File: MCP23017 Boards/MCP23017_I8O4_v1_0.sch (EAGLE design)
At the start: 71 parts, among them IC3 74HC540N, IC4 74HC540N, IC5 MCP23017SP, X4 057-016-0

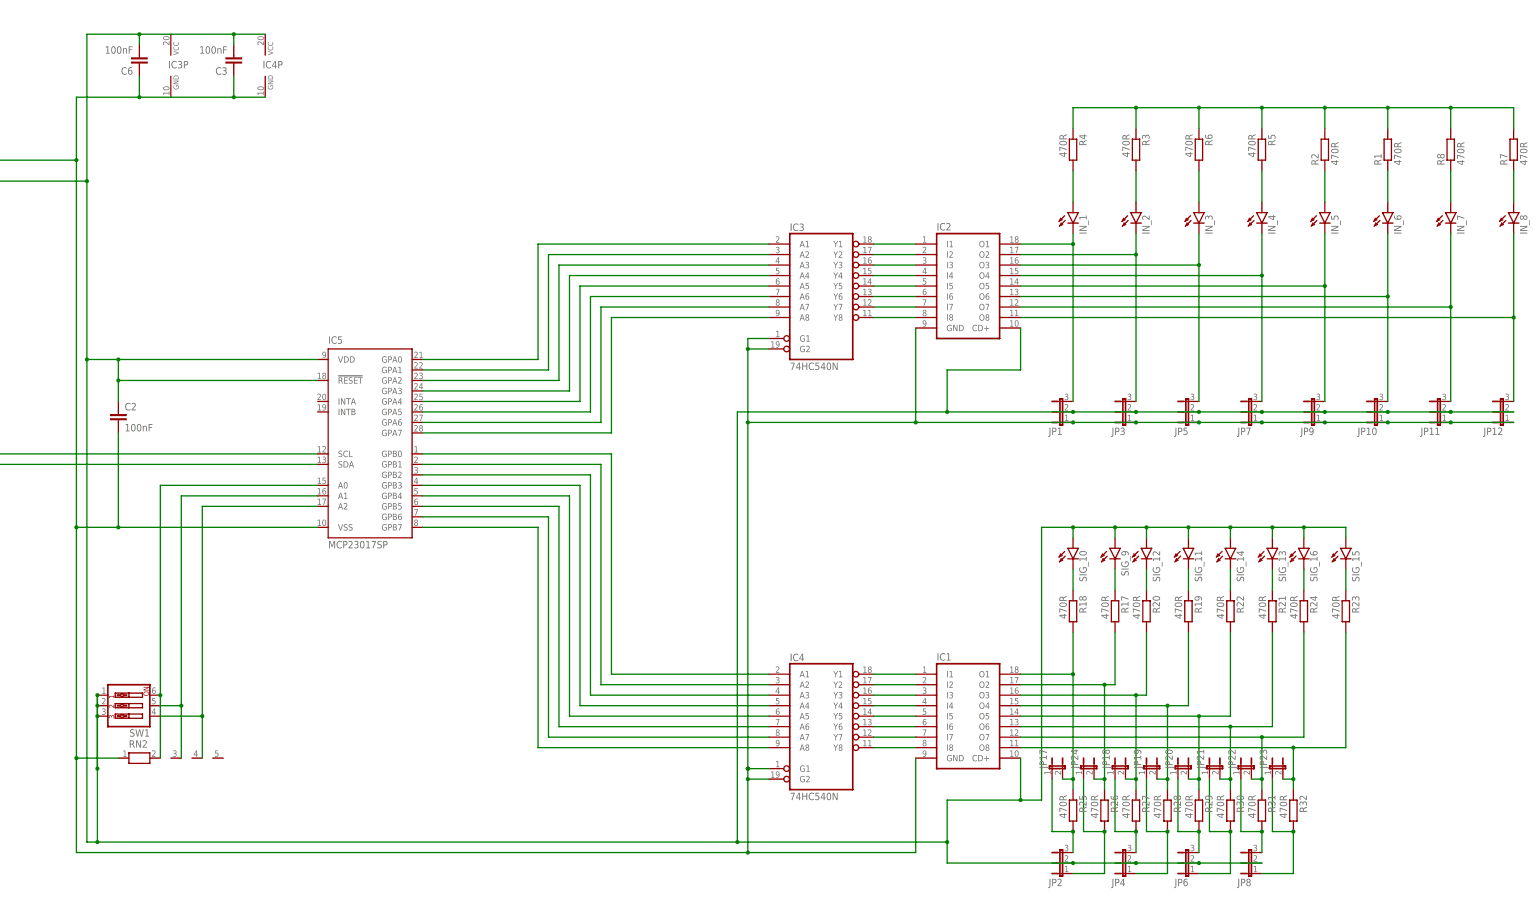
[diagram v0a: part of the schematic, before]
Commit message: Update MCP23017_I8O4_v1_0.sch
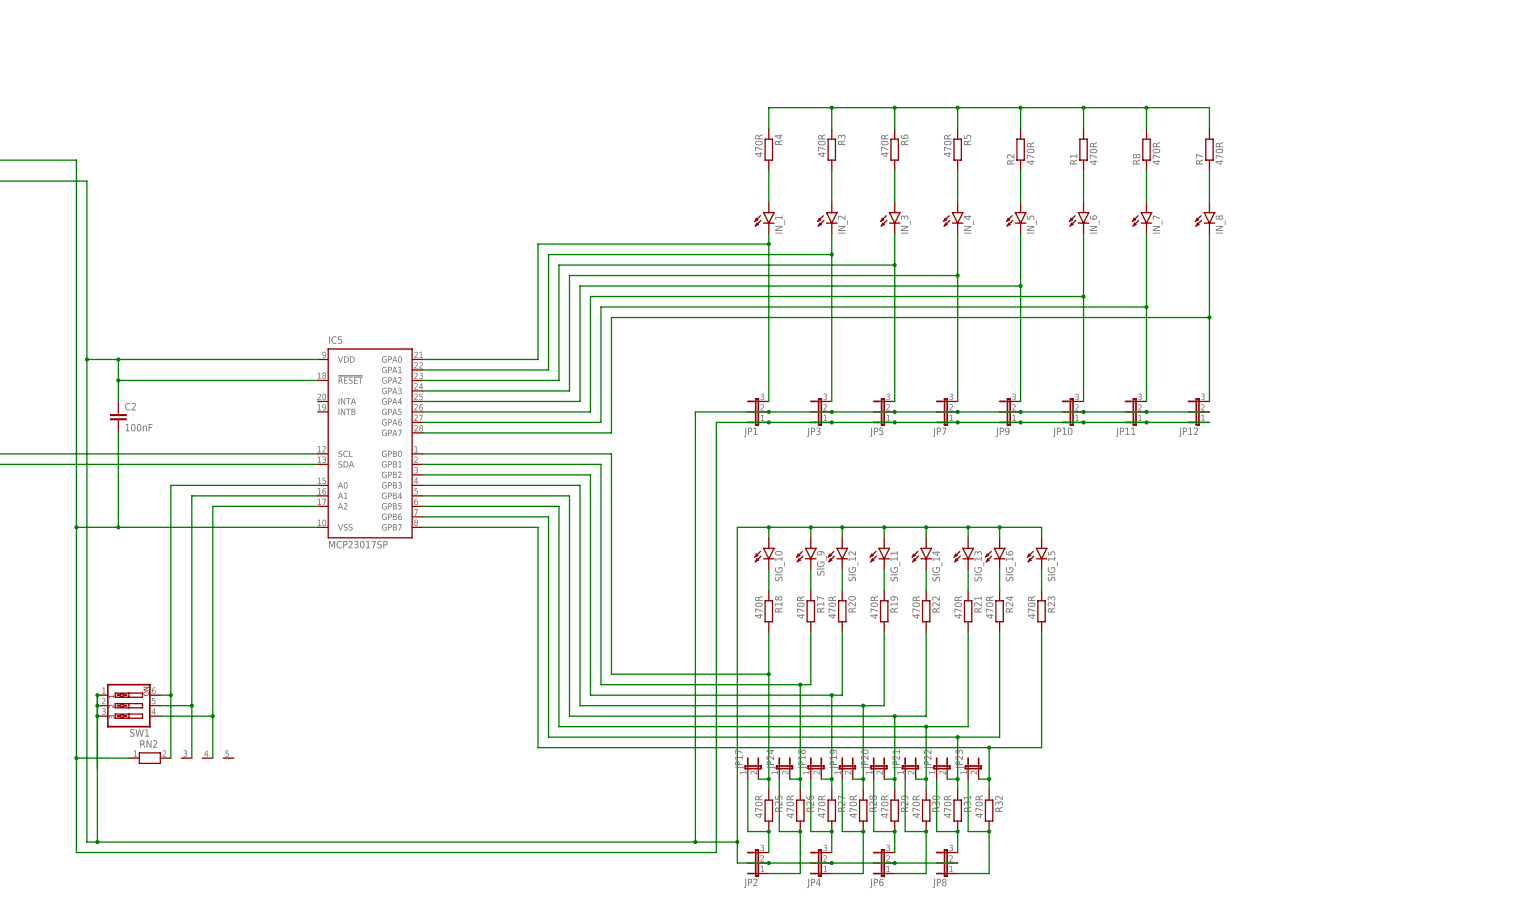
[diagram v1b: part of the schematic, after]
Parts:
- removed C3, C6: 100nF, resistor:C-EU025-024X044
- removed IC1, IC2: (no value), uln-udn:ULN2803A
- removed IC3, IC4: 74HC540N, 74xx-eu:74HC540N
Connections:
- removed net N$1: IC2.O1, IN_1.C, JP1.3
- removed net N$12: IC2.I8, IC3A.Y8
- removed net N$14: IC2.I7, IC3A.Y7
- removed net N$15: IC2.I6, IC3A.Y6
- removed net N$16: IC2.I5, IC3A.Y5
- removed net N$17: IC2.I4, IC3A.Y4
- removed net N$18: IC2.I3, IC3A.Y3
- removed net N$19: IC2.I2, IC3A.Y2
- removed net N$20: IC2.I1, IC3A.Y1
- removed net N$22: IC3A.A2, IC5.GPA1
- removed net N$24: IC3A.A4, IC5.GPA3
- removed net N$26: IC3A.A6, IC5.GPA5
- removed net N$28: IC3A.A8, IC5.GPA7
- removed net N$3: IC2.O3, IN_3.C, JP5.3
- removed net N$34: IC1.I8, IC4A.Y8
- removed net N$39: IC1.I7, IC4A.Y7
- removed net N$40: IC1.I6, IC4A.Y6
- removed net N$44: IC1.I5, IC4A.Y5
- removed net N$45: IC1.I4, IC4A.Y4
- removed net N$46: IC1.I3, IC4A.Y3
- removed net N$47: IC1.I2, IC4A.Y2
- removed net N$48: IC1.I1, IC4A.Y1
- removed net N$49: IC4A.A1, IC5.GPB0
- removed net N$5: IC2.O5, IN_5.C, JP9.3
- removed net N$51: IC4A.A3, IC5.GPB2
- removed net N$55: IC4A.A5, IC5.GPB4
- removed net N$57: IC4A.A7, IC5.GPB6
- removed net N$60: IC1.O2, JP24.2, R17.2, R26.1
- removed net N$64: IC1.O4, JP19.2, R19.2, R28.1
- removed net N$68: IC1.O6, JP21.2, R21.2, R30.1
- removed net N$8: IC2.O7, IN_7.C, JP11.3
- removed net N$83: IC1.O8, JP23.2, R23.2, R32.1
- net GND2: no longer C3.1, C6.1, IC1.GND, IC2.GND, IC3A.G1, IC3A.G2, IC3P.GND, IC4A.G1, IC4A.G2, IC4P.GND
- net N$2: now also IC5.GPA1; no longer IC2.O2
- net N$21: now also IN_1.C, JP1.3; no longer IC3A.A1
- net N$23: now also IN_3.C, JP5.3; no longer IC3A.A3
- net N$25: now also IN_5.C, JP9.3; no longer IC3A.A5
- net N$27: now also IN_7.C, JP11.3; no longer IC3A.A7
- net N$4: now also IC5.GPA3; no longer IC2.O4
- net N$50: now also JP24.2, R17.2, R26.1; no longer IC4A.A2
- net N$52: now also JP19.2, R19.2, R28.1; no longer IC4A.A4
- net N$56: now also JP21.2, R21.2, R30.1; no longer IC4A.A6
- net N$58: now also JP23.2, R23.2, R32.1; no longer IC4A.A8
- net N$59: now also IC5.GPB0; no longer IC1.O1
- net N$63: now also IC5.GPB2; no longer IC1.O3
- net N$65: now also IC5.GPB4; no longer IC1.O5
- net N$7: now also IC5.GPA5; no longer IC2.O6
- net N$71: now also IC5.GPB6; no longer IC1.O7
- net N$9: now also IC5.GPA7; no longer IC2.O8
- net VCC5.1: no longer C3.2, C6.2, IC1.CD+, IC2.CD+, IC3P.VCC, IC4P.VCC
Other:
- moved on the sheet: IN_1, IN_2, IN_3, IN_4, IN_5, IN_6, IN_7, IN_8, JP1, JP10, JP11, JP12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

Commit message: Update MCP23017_I8O4_v1_0.sch
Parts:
- RN2: device resistor-net:RN04 -> resistor-net_edit:RN03
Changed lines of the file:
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@@
 <part name="JP24" library="jumper" library_urn="urn:adsk.eagle:library:252" deviceset="JP1E" device="" package3d_urn="urn:adsk.eagle:package:15455/1"/>
 <part name="SW1" library="special" library_urn="urn:adsk.eagle:library:367" deviceset="SW_DIP-3" device="" package3d_urn="urn:adsk.eagle:package:26663/2"/>
-<part name="RN2" library="resistor-net" library_urn="urn:adsk.eagle:library:343" deviceset="RN04" device="" package3d_urn="urn:adsk.eagle:package:24976/1"/>
+<part name="RN2" library="resistor-net_edit" deviceset="RN03" device=""/>
 <part name="IC5" library="microchip-6" deviceset="MCP23017" device="SP"/>
 <part name="R3" library="resistor" library_urn="urn:adsk.eagle:library:348" deviceset="R-EU_" device="0309/10" package3d_urn="urn:adsk.eagle:package:23567/1" value="470R"/>
@@
 <attribute name="VALUE" x="78.74" y="-48.26" size="1.778" layer="96" rot="R180"/>
 </instance>
-<instance part="RN2" gate="1" x="78.74" y="-68.58" smashed="yes">
+<instance part="RN2" gate="G$1" x="78.74" y="-68.58" smashed="yes">
 <attribute name="NAME" x="76.2" y="-66.04" size="1.778" layer="95"/>
 <attribute name="VALUE" x="76.2" y="-72.898" size="1.778" layer="96"/>
@@
 <wire x1="33.02" y1="76.2" x2="60.96" y2="76.2" width="0.1524" layer="91"/>
 <junction x="33.02" y="83.82"/>
-<pinref part="RN2" gate="1" pin="1"/>
+<pinref part="RN2" gate="G$1" pin="1"/>
 <wire x1="215.9" y1="-91.44" x2="215.9" y2="12.7" width="0.1524" layer="91"/>
 <wire x1="73.66" y1="-68.58" x2="60.96" y2="-68.58" width="0.1524" layer="91"/>
@@
 <pinref part="SW1" gate="A" pin="4"/>
 <wire x1="81.28" y1="-58.42" x2="93.98" y2="-58.42" width="0.1524" layer="91"/>
-<pinref part="RN2" gate="1" pin="4"/>
+<pinref part="RN2" gate="G$1" pin="4"/>
 <wire x1="93.98" y1="-68.58" x2="93.98" y2="-58.42" width="0.1524" layer="91"/>
 <junction x="93.98" y="-58.42"/>
@@
 <pinref part="SW1" gate="A" pin="5"/>
 <wire x1="81.28" y1="-55.88" x2="88.9" y2="-55.88" width="0.1524" layer="91"/>
-<pinref part="RN2" gate="1" pin="3"/>
+<pinref part="RN2" gate="G$1" pin="3"/>
 <wire x1="88.9" y1="-68.58" x2="88.9" y2="-55.88" width="0.1524" layer="91"/>
 <junction x="88.9" y="-55.88"/>
@@
 <pinref part="SW1" gate="A" pin="6"/>
 <wire x1="83.82" y1="-53.34" x2="81.28" y2="-53.34" width="0.1524" layer="91"/>
-<pinref part="RN2" gate="1" pin="2"/>
+<pinref part="RN2" gate="G$1" pin="2"/>
 <wire x1="83.82" y1="-53.34" x2="83.82" y2="-68.58" width="0.1524" layer="91"/>
 <junction x="83.82" y="-53.34"/>
